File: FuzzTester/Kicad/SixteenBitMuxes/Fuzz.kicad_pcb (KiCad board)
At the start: 2 copper layers, 100 x 82 mm, 148 parts, among them J1 Audio In/Out JST XH, J10 Key Pad JST XH, J11 LCD JST XH, J12 Bypass Switch JST XH, J2 POT B10K JST XH, J3 POT B5K JST XH, J4 VOL POT A100K JST XH, J5 PowerTest_PinHeader, J6 9V Power JST XH, J7 Boot Reset PinHeader, J8 SPI Test PinHeader, J9 SWD_PinHeader, Q1 PN2222A, Q10 2SC1815, Q11 S8050, Q12 S9013, Q13 S9014, Q14 S9018, Q15 BC848B, Q16 2SC1623, Q17 MPSA18, Q18 MPSA18, Q19 2N5088, Q2 MMBT3904, Q20 2N5088, Q21 PN2222A, Q22 MMBT3904, Q23 MMBT5551L, Q24 MMBTA42, Q25 BC807, Q26 BC846, Q27 BC847B, Q28 BC847C, Q29 C945, Q3 MMBT5551L, Q30 2SC1815, Q31 S8050, Q32 S9013, Q33 S9014, Q34 S9018, Q35 BC848B, Q36 2SC1623, Q37 MPSA18, Q38 MPSA18, Q39 2N5088, Q4 MMBTA42, Q40 2N5088, Q5 BC807, Q6 BC846, Q7 BC847B, Q8 BC847C, Q9 C945, U1 AMS1117-5.0, U10 CD4052B, U11 CD4052B, U12 CD4052B, U13 CD4052B, U14 CD4051B, U15 CD4052B, U16 CD4051B, U17 CD4052B, U18 CD4052B, U19 CD4052B, U2 AMS1117-3.3, U20 74HC595, U21 CD4051B, U22 4504, U23 4504, U24 4504, U25 CD4053B, U3 STM32F103C8Tx, U4 CD4051B, U5 74HC595, U6 CD4052B, U7 CD4051B, U8 CD4052B, U9 CD4051B, Y1 8MHz

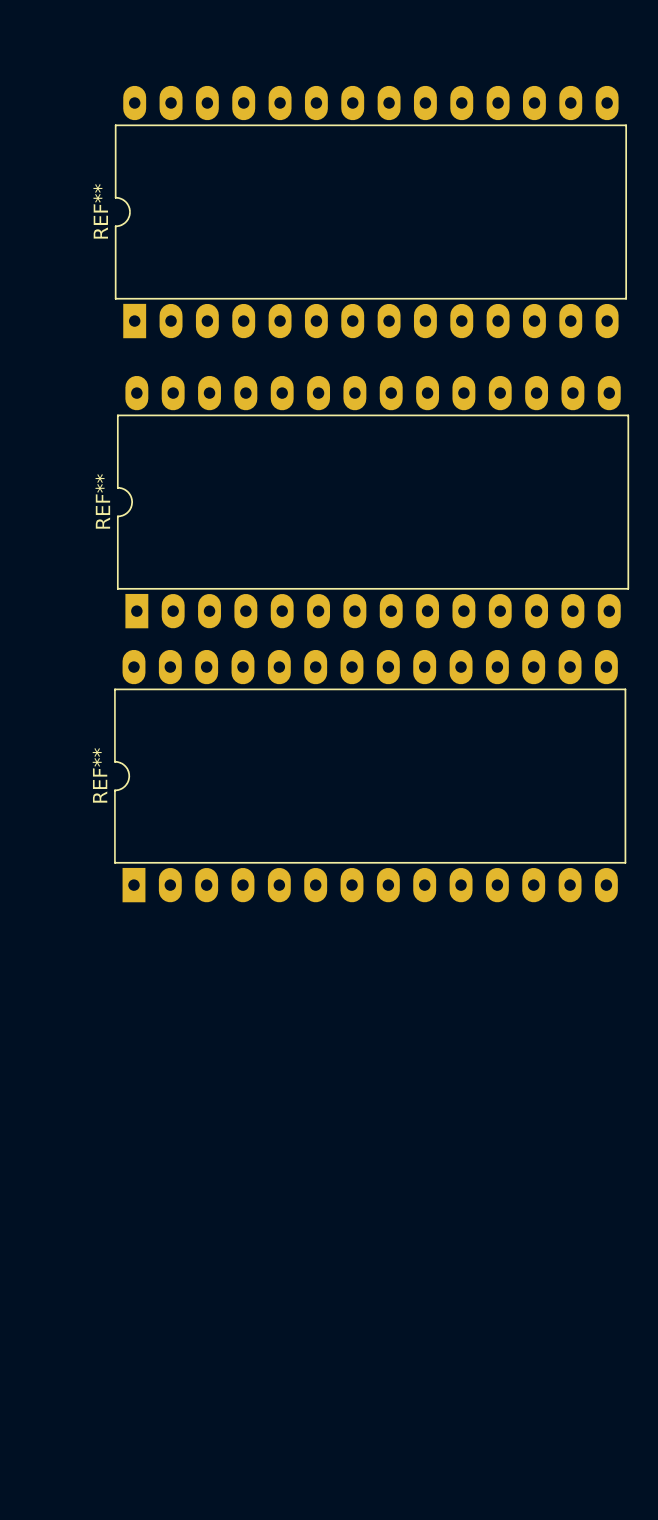
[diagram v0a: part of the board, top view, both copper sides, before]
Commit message: Removed shift registers
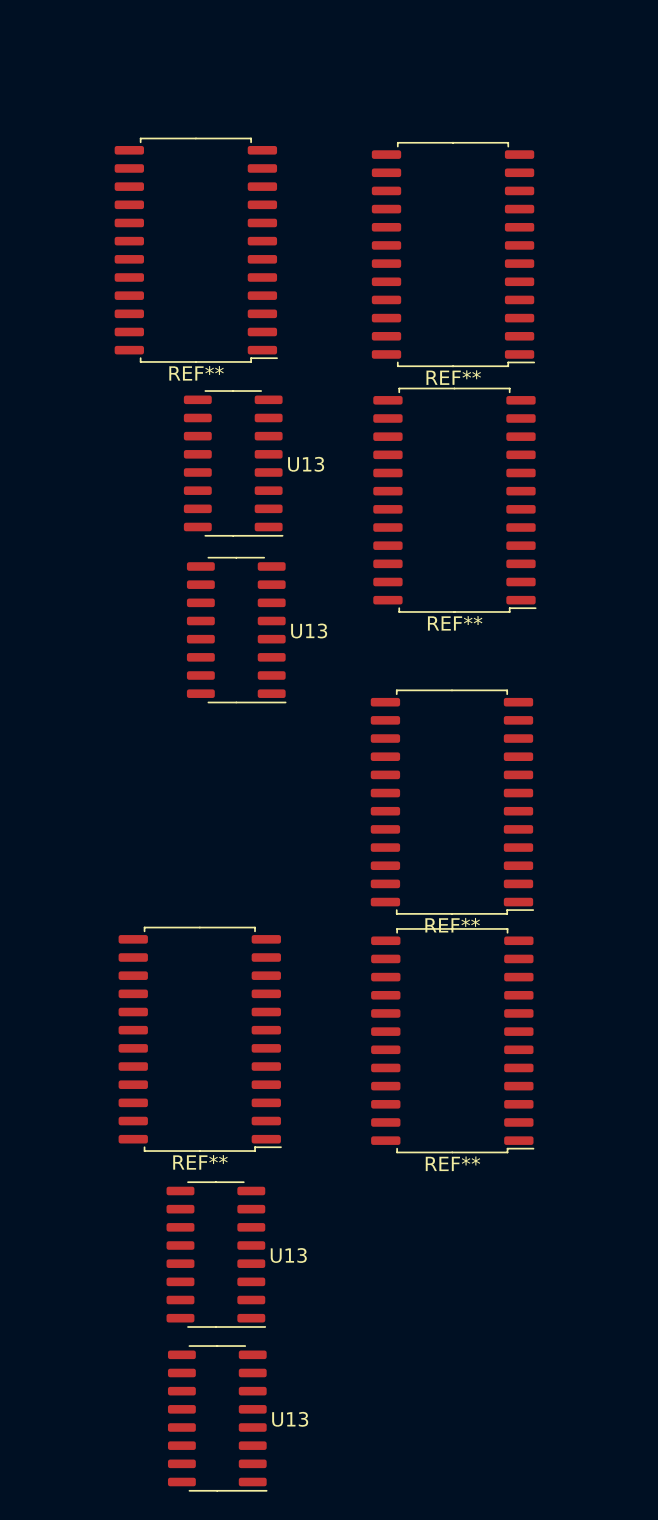
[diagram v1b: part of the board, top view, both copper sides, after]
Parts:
- removed the REF** at (152.0, 91.1)
- removed the REF** at (152.1, 51.6)
- removed the REF** at (152.2, 71.9)
- added REF**: SOIC-24W_7.5x15.4mm_P1.27mm, Package_SO:SOIC-24W_7.5x15.4mm_P1.27mm, F.Cu at (156.3, 46.7)
- added REF**: SOIC-24W_7.5x15.4mm_P1.27mm, Package_SO:SOIC-24W_7.5x15.4mm_P1.27mm, F.Cu at (156.6, 101.8)
- added REF**: SOIC-24W_7.5x15.4mm_P1.27mm, Package_SO:SOIC-24W_7.5x15.4mm_P1.27mm, F.Cu at (174.3, 47.0)
- added REF**: SOIC-24W_7.5x15.4mm_P1.27mm, Package_SO:SOIC-24W_7.5x15.4mm_P1.27mm, F.Cu at (174.4, 64.2)
- added REF**: SOIC-24W_7.5x15.4mm_P1.27mm, Package_SO:SOIC-24W_7.5x15.4mm_P1.27mm, F.Cu at (174.2, 102.0)
- added REF**: SOIC-24W_7.5x15.4mm_P1.27mm, Package_SO:SOIC-24W_7.5x15.4mm_P1.27mm, F.Cu at (174.2, 85.3)
- added U13: CD4052B, Package_SO:SOIC-16_3.9x9.9mm_P1.27mm, F.Cu at (157.7, 116.9)
- added U13: CD4052B, Package_SO:SOIC-16_3.9x9.9mm_P1.27mm, F.Cu at (157.8, 128.3)
- added U13: CD4052B, Package_SO:SOIC-16_3.9x9.9mm_P1.27mm, F.Cu at (158.9, 61.6)
- added U13: CD4052B, Package_SO:SOIC-16_3.9x9.9mm_P1.27mm, F.Cu at (159.2, 73.2)

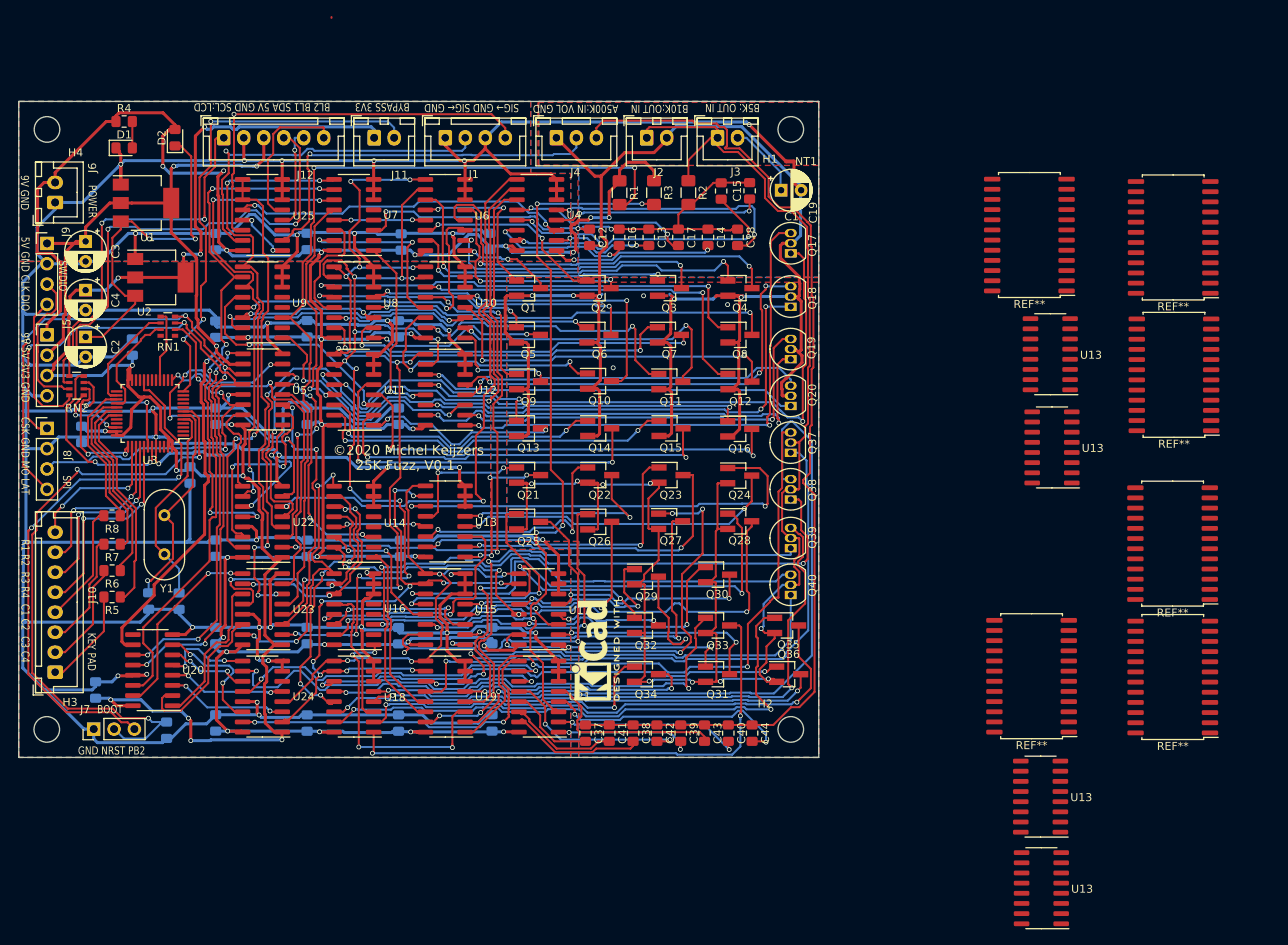
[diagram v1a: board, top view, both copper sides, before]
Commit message: Finished (but not beautiful) PCB without SPI and most 8 channel multiplexers.
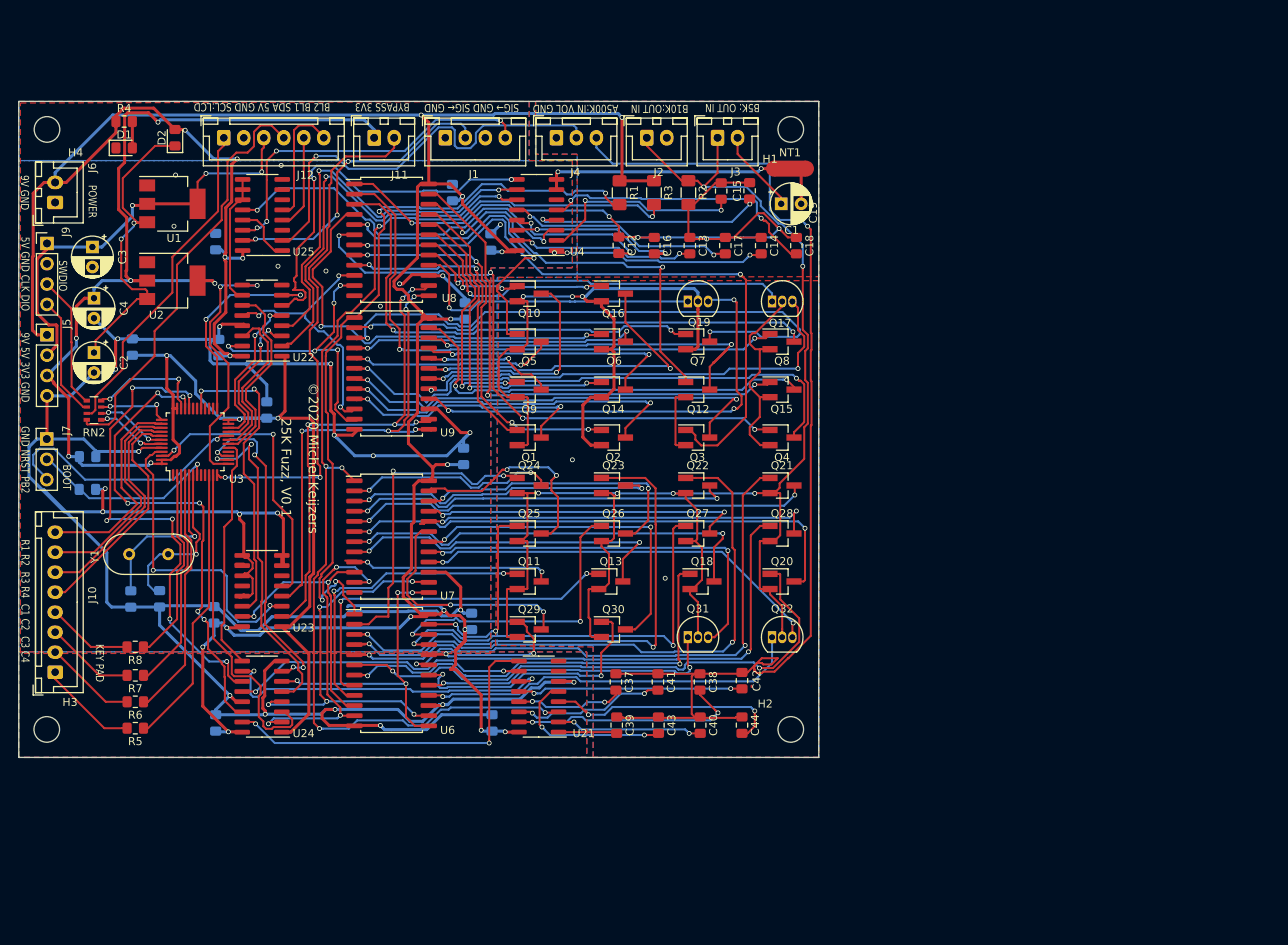
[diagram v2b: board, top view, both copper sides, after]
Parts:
- removed C20, C25, C26, C27, C28, C29, C30, C31, C32, C33, C34, C35: 100nF, Capacitor_SMD:C_0805_2012Metric_Pad1.15x1.40mm_HandSolder
- removed J8: SPI Test PinHeader, Connector_PinHeader_2.54mm:PinHeader_1x04_P2.54mm_Vertical
- removed Q33: S9014, Package_TO_SOT_SMD:SOT-23_Handsoldering
- removed Q34: S9018, Package_TO_SOT_SMD:SOT-23_Handsoldering
- removed Q35: BC848B, Package_TO_SOT_SMD:SOT-23_Handsoldering
- removed Q36: 2SC1623, Package_TO_SOT_SMD:SOT-23_Handsoldering
- removed Q37, Q38: MPSA18, Package_TO_SOT_THT:TO-92_Inline
- removed Q39, Q40: 2N5088, Package_TO_SOT_THT:TO-92_Inline
- removed REF** (x6): SOIC-24W_7.5x15.4mm_P1.27mm, Package_SO:SOIC-24W_7.5x15.4mm_P1.27mm
- removed REF**: KiCad-Logo2_20mm_SilkScreen, Symbol:KiCad-Logo2_20mm_SilkScreen
- removed REF**: KiCad-Logo2_5mm_SilkScreen, Symbol:KiCad-Logo2_5mm_SilkScreen
- removed RN1: R_Pack04, Resistor_SMD:R_Array_Convex_4x0603
- removed U10, U11, U12, U13 (x5), U15, U17, U18, U19: CD4052B, Package_SO:SOIC-16_3.9x9.9mm_P1.27mm
- removed U14, U16: CD4051B, Package_SO:SOIC-16_3.9x9.9mm_P1.27mm
- removed U20, U5: 74HC595, Package_SO:SOIC-16_3.9x9.9mm_P1.27mm
- NT1: footprint NetTie:NetTie-2_SMD_Pad0.5mm -> NetTie:NetTie-2_SMD_Pad2.0mm
- Q11: value S8050 -> PN2222A
- Q13: value S9014 -> MMBT3904
- Q18: value MPSA18 -> MMBT5551L; footprint Package_TO_SOT_THT:TO-92_Inline -> Package_TO_SOT_SMD:SOT-23_Handsoldering
- Q20: value 2N5088 -> MMBTA42; footprint Package_TO_SOT_THT:TO-92_Inline -> Package_TO_SOT_SMD:SOT-23_Handsoldering
- Q21: value PN2222A -> BC807
- Q22: value MMBT3904 -> BC846
- Q23: value MMBT5551L -> BC847B
- Q24: value MMBTA42 -> BC847C
- Q25: value BC807 -> BC848B
- Q26: value BC846 -> S9013
- Q27: value BC847B -> S9018
- Q28: value BC847C -> C945
- Q29: value C945 -> 2SC1623
- Q31: value S8050 -> MPSA18; footprint Package_TO_SOT_SMD:SOT-23_Handsoldering -> Package_TO_SOT_THT:TO-92_Inline
- Q32: value S9013 -> 2N5088; footprint Package_TO_SOT_SMD:SOT-23_Handsoldering -> Package_TO_SOT_THT:TO-92_Inline
- U6, U8: value CD4052B -> CD4067BM; footprint Package_SO:SOIC-16_3.9x9.9mm_P1.27mm -> Package_SO:SOIC-24W_7.5x15.4mm_P1.27mm
- U7, U9: value CD4051B -> CD4067BM; footprint Package_SO:SOIC-16_3.9x9.9mm_P1.27mm -> Package_SO:SOIC-24W_7.5x15.4mm_P1.27mm
- moved U6 57.3 mm to (76.6, 101.1), turned to 0 degrees
- moved C21 48.2 mm to (86.6, 95.0)
- moved U7 40.5 mm to (76.6, 84.4), turned to 0 degrees
- moved J7 36.7 mm to (33.5, 72.2), turned to 0 degrees
- moved Q18 36.1 mm to (115.4, 90.0), turned to 0 degrees
- moved C22 33.2 mm to (85.6, 74.4)
- moved Q21 31.7 mm to (125.4, 78.0)
- moved C10 31.7 mm to (38.6, 78.5), turned to 0 degrees
- moved Q11 30.6 mm to (93.8, 90.0)
- moved Q24 26.3 mm to (93.8, 78.0)
- moved U22 25.2 mm to (60.4, 57.4)
- moved C47 25.1 mm to (55.0, 60.8)
- moved Q16 23.1 mm to (104.3, 54.0)
- moved Q20 22.0 mm to (125.4, 90.0), turned to 0 degrees
- moved Q13 21.7 mm to (104.0, 90.0)
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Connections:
- J9 pad 3: /Mcu/SYS_JTICK_SWCLK -> /Mcu/SYS_JTMS_SWDIO
- J9 pad 4: /Mcu/SYS_JTMS_SWDIO -> /Mcu/SYS_JTICK_SWCLK
- Q10 pad 1: /TransistorsB/10_BASE -> /TransistorsB/14_BASE
- Q10 pad 3: /TransistorsB/10_COLLECTOR -> /TransistorsB/14_COLLECTOR
- Q11 pad 1: /TransistorsB/11_BASE -> /TransistorsC/1_BASE
- Q11 pad 2: GNDA -> /TransistorsC/EMITTER
- Q11 pad 3: /TransistorsB/11_COLLECTOR -> /TransistorsC/1_COLLECTOR
- Q12 pad 1: /TransistorsB/12_BASE -> /TransistorsB/10_BASE
- Q12 pad 3: /TransistorsB/12_COLLECTOR -> /TransistorsB/10_COLLECTOR
- Q13 pad 1: /TransistorsB/13_BASE -> /TransistorsC/2_BASE
- Q13 pad 2: GNDA -> /TransistorsC/EMITTER
- Q13 pad 3: /TransistorsB/13_COLLECTOR -> /TransistorsC/2_COLLECTOR
- Q14 pad 1: /TransistorsB/14_BASE -> /TransistorsB/11_BASE
- Q14 pad 3: /TransistorsB/14_COLLECTOR -> /TransistorsB/11_COLLECTOR
- Q15 pad 1: /TransistorsB/15_BASE -> /TransistorsB/9_BASE
- Q15 pad 3: /TransistorsB/15_COLLECTOR -> /TransistorsB/9_COLLECTOR
- Q16 pad 1: /TransistorsB/16_BASE -> /TransistorsB/13_BASE
- Q16 pad 3: /TransistorsB/16_COLLECTOR -> /TransistorsB/13_COLLECTOR
- Q17 pad 1: /TransistorsB/17_BASE -> /TransistorsB/15_BASE
- Q17 pad 3: /TransistorsB/17_COLLECTOR -> /TransistorsB/15_COLLECTOR
- Q18 pad 1: /TransistorsB/18_BASE -> /TransistorsC/3_BASE
- Q18 pad 2: GNDA -> /TransistorsC/EMITTER
- Q18 pad 3: /TransistorsB/18_COLLECTOR -> /TransistorsC/3_COLLECTOR
- Q19 pad 1: /TransistorsB/19_BASE -> /TransistorsB/16_BASE
- Q19 pad 3: /TransistorsB/19_COLLECTOR -> /TransistorsB/16_COLLECTOR
- Q20 pad 1: /TransistorsB/20_BASE -> /TransistorsC/4_BASE
- Q20 pad 2: GNDA -> /TransistorsC/EMITTER
- Q20 pad 3: /TransistorsB/20_COLLECTOR -> /TransistorsC/4_COLLECTOR
- Q21 pad 1: /TransistorsC/1_BASE -> /TransistorsC/5_BASE
- Q21 pad 3: /TransistorsC/1_COLLECTOR -> /TransistorsC/5_COLLECTOR
- Q22 pad 1: /TransistorsC/2_BASE -> /TransistorsC/6_BASE
- Q22 pad 3: /TransistorsC/2_COLLECTOR -> /TransistorsC/6_COLLECTOR
- Q23 pad 1: /TransistorsC/3_BASE -> /TransistorsC/7_BASE
- Q23 pad 3: /TransistorsC/3_COLLECTOR -> /TransistorsC/7_COLLECTOR
- Q24 pad 1: /TransistorsC/4_BASE -> /TransistorsC/8_BASE
- Q24 pad 3: /TransistorsC/4_COLLECTOR -> /TransistorsC/8_COLLECTOR
- Q25 pad 1: /TransistorsC/5_BASE -> /TransistorsC/9_BASE
- Q25 pad 3: /TransistorsC/5_COLLECTOR -> /TransistorsC/9_COLLECTOR
- Q26 pad 1: /TransistorsC/6_BASE -> /TransistorsC/10_BASE
- Q26 pad 3: /TransistorsC/6_COLLECTOR -> /TransistorsC/10_COLLECTOR
- Q27 pad 1: /TransistorsC/7_BASE -> /TransistorsC/11_BASE
- Q27 pad 3: /TransistorsC/7_COLLECTOR -> /TransistorsC/11_COLLECTOR
- Q28 pad 1: /TransistorsC/8_BASE -> /TransistorsC/12_BASE
- Q28 pad 3: /TransistorsC/8_COLLECTOR -> /TransistorsC/12_COLLECTOR
- Q29 pad 1: /TransistorsC/9_BASE -> /TransistorsC/13_BASE
- Q29 pad 3: /TransistorsC/9_COLLECTOR -> /TransistorsC/13_COLLECTOR
- Q30 pad 1: /TransistorsC/10_BASE -> /TransistorsC/14_BASE
- Q30 pad 3: /TransistorsC/10_COLLECTOR -> /TransistorsC/14_COLLECTOR
- Q31 pad 1: /TransistorsC/11_BASE -> /TransistorsC/15_BASE
- Q31 pad 3: /TransistorsC/11_COLLECTOR -> /TransistorsC/15_COLLECTOR
- Q32 pad 1: /TransistorsC/12_BASE -> /TransistorsC/16_BASE
- Q32 pad 3: /TransistorsC/12_COLLECTOR -> /TransistorsC/16_COLLECTOR
- Q9 pad 1: /TransistorsB/9_BASE -> /TransistorsB/12_BASE
- Q9 pad 3: /TransistorsB/9_COLLECTOR -> /TransistorsB/12_COLLECTOR
- RN2 pad 1: /Mcu/SYS_JTMS_SWDIO_MCU -> /Mcu/I2C1_SDA_MCU
- RN2 pad 2: /Mcu/SYS_JTICK_SWCLK_MCU -> /Mcu/I2C1_SCL_MCU
- RN2 pad 3: /Mcu/I2C1_SCL_MCU -> /Mcu/SYS_JTICK_SWCLK_MCU
- RN2 pad 4: /Mcu/I2C1_SDA_MCU -> /Mcu/SYS_JTMS_SWDIO_MCU
- RN2 pad 5: /Mcu/I2C1_SDA -> /Mcu/SYS_JTMS_SWDIO
- RN2 pad 6: /Mcu/I2C1_SCL -> /Mcu/SYS_JTICK_SWCLK
- RN2 pad 7: /Mcu/SYS_JTICK_SWCLK -> /Mcu/I2C1_SCL
- RN2 pad 8: /Mcu/SYS_JTMS_SWDIO -> /Mcu/I2C1_SDA
- U22 pad 10: /TRANSISTOR_B_GROUP_SELECTION_0 -> /BYPASS_MODE
- U22 pad 11: /TRANSISTOR_B_GROUP_SELECTION_3V3_1 -> /TRANSISTOR_B_SELECTION_0_3V3
- U22 pad 12: /TRANSISTOR_B_GROUP_SELECTION_1 -> /TRANSISTOR_B_SELECTION_0
- U22 pad 14: /TRANSISTOR_B_GROUP_SELECTION_3V3_2 -> /TRANSISTOR_B_SELECTION_1_3V3
- U22 pad 15: /TRANSISTOR_B_GROUP_SELECTION_2 -> /TRANSISTOR_B_SELECTION_1
- U22 pad 3: /CAPACITOR_A_SELECTION_3V3_0 -> /CAPACITOR_A_SELECTION_0_3V3
- U22 pad 5: /CAPACITOR_A_SELECTION_3V3_1 -> /CAPACITOR_A_SELECTION_1_3V3
- U22 pad 7: /CAPACITOR_A_SELECTION_3V3_2 -> /CAPACITOR_A_SELECTION_2_3V3
- U22 pad 9: /TRANSISTOR_B_GROUP_SELECTION_3V3_0 -> /BYPASS_MODE_3V3
- U23 pad 10: /TRANSISTOR_C_GROUP_SELECTION_0 -> Net-(U23-Pad10)
- U23 pad 11: /TRANSISTOR_C_GROUP_SELECTION_3V3_1 -> GND
- U23 pad 12: /TRANSISTOR_C_GROUP_SELECTION_1 -> Net-(U23-Pad12)
- U23 pad 14: /TRANSISTOR_C_GROUP_SELECTION_3V3_2 -> /TRANSISTOR_C_SELECTION_0_3V3
- U23 pad 15: /TRANSISTOR_C_GROUP_SELECTION_2 -> /TRANSISTOR_C_SELECTION_0
- U23 pad 2: /TRANSISTOR_B_SELECTION_0 -> /TRANSISTOR_B_SELECTION_2
- U23 pad 3: /TRANSISTOR_B_SELECTION_3V3_0 -> /TRANSISTOR_B_SELECTION_2_3V3
- U23 pad 4: /TRANSISTOR_B_SELECTION_1 -> /TRANSISTOR_B_SELECTION_3
- U23 pad 5: /TRANSISTOR_B_SELECTION_3V3_1 -> /TRANSISTOR_B_SELECTION_3_3V3
- U23 pad 6: /BYPASS_MODE -> Net-(U23-Pad6)
- U23 pad 7: /BYPASS_MODE_3V3 -> GND
- U23 pad 9: /TRANSISTOR_C_GROUP_SELECTION_3V3_0 -> GND
- U24 pad 11: /CAPACITOR_D_SELECTION_3V3_1 -> /CAPACITOR_D_SELECTION_1_3V3
- U24 pad 14: /CAPACITOR_D_SELECTION_3V3_2 -> /CAPACITOR_D_SELECTION_2_3V3
- U24 pad 2: /TRANSISTOR_C_SELECTION_0 -> /TRANSISTOR_C_SELECTION_1
- U24 pad 3: /TRANSISTOR_C_SELECTION_3V3_0 -> /TRANSISTOR_C_SELECTION_1_3V3
- U24 pad 4: /TRANSISTOR_C_SELECTION_1 -> /TRANSISTOR_C_SELECTION_2
- U24 pad 5: /TRANSISTOR_C_SELECTION_3V3_1 -> /TRANSISTOR_C_SELECTION_2_3V3
- U24 pad 6: Net-(U24-Pad6) -> /TRANSISTOR_C_SELECTION_3
- U24 pad 7: GND -> /TRANSISTOR_C_SELECTION_3_3V3
- U24 pad 9: /CAPACITOR_D_SELECTION_3V3_0 -> /CAPACITOR_D_SELECTION_0_3V3
- U3 pad 10: Net-(U3-Pad10) -> /Mcu/GPIO_KEYPAD_COLUMN_1
- U3 pad 11: Net-(U3-Pad11) -> /TRANSISTOR_C_SELECTION_1_3V3
- U3 pad 14: Net-(U3-Pad14) -> /TRANSISTOR_C_SELECTION_2_3V3
- U3 pad 15: Net-(U3-Pad15) -> /TRANSISTOR_C_SELECTION_3_3V3
- U3 pad 16: /Mcu/GPIO_LATCH_MCU -> Net-(U3-Pad16)
- U3 pad 17: Net-(U3-Pad17) -> /CAPACITOR_D_SELECTION_0_3V3
- U3 pad 18: Net-(U3-Pad18) -> /TRANSISTOR_B_SELECTION_0_3V3
- U3 pad 19: Net-(U3-Pad19) -> /TRANSISTOR_B_SELECTION_1_3V3
- U3 pad 2: Net-(U3-Pad2) -> /Mcu/GPIO_KEYPAD_COLUMN_4
- U3 pad 21: Net-(U3-Pad21) -> /CAPACITOR_A_SELECTION_0_3V3
- U3 pad 22: Net-(U3-Pad22) -> /CAPACITOR_A_SELECTION_1_3V3
- U3 pad 25: Net-(U3-Pad25) -> /CAPACITOR_A_SELECTION_2_3V3
- U3 pad 26: /Mcu/SPI2_CSK_MCU -> Net-(U3-Pad26)
- U3 pad 27: /Mcu/GPIO_KEYPAD_COLUMN_4 -> Net-(U3-Pad27)
- U3 pad 28: /Mcu/SPI2_MOSI_MCU -> Net-(U3-Pad28)
- U3 pad 29: /Mcu/GPIO_KEYPAD_COLUMN_3 -> /TRANSISTOR_C_SELECTION_0_3V3
- U3 pad 3: Net-(U3-Pad3) -> /Mcu/GPIO_KEYPAD_COLUMN_3
- U3 pad 30: /Mcu/GPIO_KEYPAD_COLUMN_2 -> Net-(U3-Pad30)
- U3 pad 31: /Mcu/GPIO_KEYPAD_COLUMN_1 -> Net-(U3-Pad31)
- U3 pad 32: Net-(U3-Pad32) -> /CAPACITOR_D_SELECTION_1_3V3
- U3 pad 33: Net-(U3-Pad33) -> /CAPACITOR_D_SELECTION_2_3V3
- U3 pad 4: Net-(U3-Pad4) -> /Mcu/GPIO_KEYPAD_COLUMN_2
- U3 pad 45: Net-(U3-Pad45) -> /TRANSISTOR_B_SELECTION_2_3V3
- U3 pad 46: Net-(U3-Pad46) -> /TRANSISTOR_B_SELECTION_3_3V3
- U6 pad 1: /TransistorsB/1_COLLECTOR -> /TransistorsC/BASE
- U6 pad 10: /TRANSISTOR_B_SELECTION_0 -> /TRANSISTOR_C_SELECTION_0
- U6 pad 11: /TransistorsB/4_BASE -> /TRANSISTOR_C_SELECTION_1
- U6 pad 12: /TransistorsB/1_BASE -> GND
- U6 pad 13: /TransistorsB/TG_1_BASE -> /TRANSISTOR_C_SELECTION_3
- U6 pad 14: /TransistorsB/2_BASE -> /TRANSISTOR_C_SELECTION_2
- U6 pad 15: /TransistorsB/3_BASE -> GND
- U6 pad 16: +9V -> /TransistorsC/16_BASE
- U6 pad 2: /TransistorsB/3_COLLECTOR -> /TransistorsC/8_BASE
- U6 pad 3: /TransistorsB/TG_1_COLLECTOR -> /TransistorsC/7_BASE
- U6 pad 4: /TransistorsB/4_COLLECTOR -> /TransistorsC/6_BASE
- U6 pad 5: /TransistorsB/2_COLLECTOR -> /TransistorsC/5_BASE
- U6 pad 6: GND -> /TransistorsC/4_BASE
- U6 pad 7: GND -> /TransistorsC/3_BASE
- U6 pad 8: GND -> /TransistorsC/2_BASE
- U6 pad 9: /TRANSISTOR_B_SELECTION_1 -> /TransistorsC/1_BASE
- U7 pad 1: /TransistorsB/TG_5_BASE -> /CapacitorsD/CAPACITOR_AUDIO_INPUT
- U7 pad 10: /TRANSISTOR_B_GROUP_SELECTION_1 -> /TRANSISTOR_C_SELECTION_0
- U7 pad 11: /TRANSISTOR_B_GROUP_SELECTION_0 -> /TRANSISTOR_C_SELECTION_1
- U7 pad 12: /TransistorsB/TG_4_BASE -> GND
- U7 pad 13: /TransistorsB/TG_1_BASE -> /TRANSISTOR_C_SELECTION_3
- U7 pad 14: /TransistorsB/TG_2_BASE -> /TRANSISTOR_C_SELECTION_2
- U7 pad 15: /TransistorsB/TG_3_BASE -> GND
- U7 pad 16: +9V -> /TransistorsC/16_COLLECTOR
- U7 pad 2: Net-(U7-Pad2) -> /TransistorsC/8_COLLECTOR
- U7 pad 3: /TransistorsB/BASE -> /TransistorsC/7_COLLECTOR
- U7 pad 4: Net-(U7-Pad4) -> /TransistorsC/6_COLLECTOR
- U7 pad 5: Net-(U7-Pad5) -> /TransistorsC/5_COLLECTOR
- U7 pad 6: GND -> /TransistorsC/4_COLLECTOR
- U7 pad 7: GND -> /TransistorsC/3_COLLECTOR
- U7 pad 8: GND -> /TransistorsC/2_COLLECTOR
- U7 pad 9: /TRANSISTOR_B_GROUP_SELECTION_2 -> /TransistorsC/1_COLLECTOR
- U8 pad 1: /TransistorsB/5_COLLECTOR -> /TransistorsB/BASE
- U8 pad 11: /TransistorsB/8_BASE -> /TRANSISTOR_B_SELECTION_1
- U8 pad 12: /TransistorsB/5_BASE -> GND
- U8 pad 13: /TransistorsB/TG_2_BASE -> /TRANSISTOR_B_SELECTION_3
- U8 pad 14: /TransistorsB/6_BASE -> /TRANSISTOR_B_SELECTION_2
- U8 pad 15: /TransistorsB/7_BASE -> GND
- U8 pad 16: +9V -> /TransistorsB/16_BASE
- U8 pad 2: /TransistorsB/7_COLLECTOR -> /TransistorsB/8_BASE
- U8 pad 3: /TransistorsB/TG_2_COLLECTOR -> /TransistorsB/7_BASE
- U8 pad 4: /TransistorsB/8_COLLECTOR -> /TransistorsB/6_BASE
- U8 pad 5: /TransistorsB/6_COLLECTOR -> /TransistorsB/5_BASE
- U8 pad 6: GND -> /TransistorsB/4_BASE
- U8 pad 7: GND -> /TransistorsB/3_BASE
- U8 pad 8: GND -> /TransistorsB/2_BASE
- U8 pad 9: /TRANSISTOR_B_SELECTION_1 -> /TransistorsB/1_BASE
- U9 pad 1: /TransistorsB/TG_5_COLLECTOR -> /TransistorsC/BASE
- U9 pad 10: /TRANSISTOR_B_GROUP_SELECTION_1 -> /TRANSISTOR_B_SELECTION_0
- U9 pad 11: /TRANSISTOR_B_GROUP_SELECTION_0 -> /TRANSISTOR_B_SELECTION_1
- U9 pad 12: /TransistorsB/TG_4_COLLECTOR -> GND
- U9 pad 13: /TransistorsB/TG_1_COLLECTOR -> /TRANSISTOR_B_SELECTION_3
- U9 pad 14: /TransistorsB/TG_2_COLLECTOR -> /TRANSISTOR_B_SELECTION_2
- U9 pad 15: /TransistorsB/TG_3_COLLECTOR -> GND
- U9 pad 16: +9V -> /TransistorsB/16_COLLECTOR
- U9 pad 2: Net-(U9-Pad2) -> /TransistorsB/8_COLLECTOR
- U9 pad 3: /TransistorsC/BASE -> /TransistorsB/7_COLLECTOR
- U9 pad 4: Net-(U9-Pad4) -> /TransistorsB/6_COLLECTOR
- U9 pad 5: Net-(U9-Pad5) -> /TransistorsB/5_COLLECTOR
- U9 pad 6: GND -> /TransistorsB/4_COLLECTOR
- U9 pad 7: GND -> /TransistorsB/3_COLLECTOR
- U9 pad 8: GND -> /TransistorsB/2_COLLECTOR
- U9 pad 9: /TRANSISTOR_B_GROUP_SELECTION_2 -> /TransistorsB/1_COLLECTOR
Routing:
- net GND: track 833.3 -> 411.6 mm, vias 36 -> 30
- net /GPIO_LATCH: track 98.9 -> 0.00 mm, vias 6 -> 0
- net /SPI2_CSK: track 91.2 -> 0.00 mm, vias 4 -> 0
- net GNDA: track 213.6 -> 124.8 mm, vias 8 -> 5
- net /TransistorsC/18_BASE: track 85.7 -> 0.00 mm, vias 2 -> 0
- net /TransistorsC/18_COLLECTOR: track 85.5 -> 0.00 mm, vias 1 -> 0
- net /TRANSISTOR_B_SELECTION_0: track 115.9 -> 33.1 mm, vias 13 -> 3
- net /TransistorsC/17_BASE: track 77.8 -> 0.00 mm, vias 1 -> 0
- net /TransistorsC/17_COLLECTOR: track 76.9 -> 0.00 mm, vias 2 -> 0
- net /TransistorsB/17_BASE: track 71.9 -> 0.00 mm, vias 2 -> 0
- net /TRANSISTOR_B_GROUP_SELECTION_1: track 69.8 -> 0.00 mm, vias 6 -> 0
- net +5V: track 123.7 -> 54.3 mm, vias 4 -> 3
- net /TRANSISTOR_B_GROUP_SELECTION_2: track 68.6 -> 0.00 mm, vias 4 -> 0
- net /TRANSISTOR_B_SELECTION_1: track 106.5 -> 38.4 mm, vias 10 -> 5
- net /TransistorsC/19_BASE: track 68.1 -> 0.00 mm, vias 3 -> 0
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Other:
- board text removed: "CSK GND MO LAT"
- board text removed: "SPI"
